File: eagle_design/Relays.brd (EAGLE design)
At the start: 81.3 x 32.7 mm, 13 parts, among them K1 G5LE, K2 G5LE, K3 G5LE

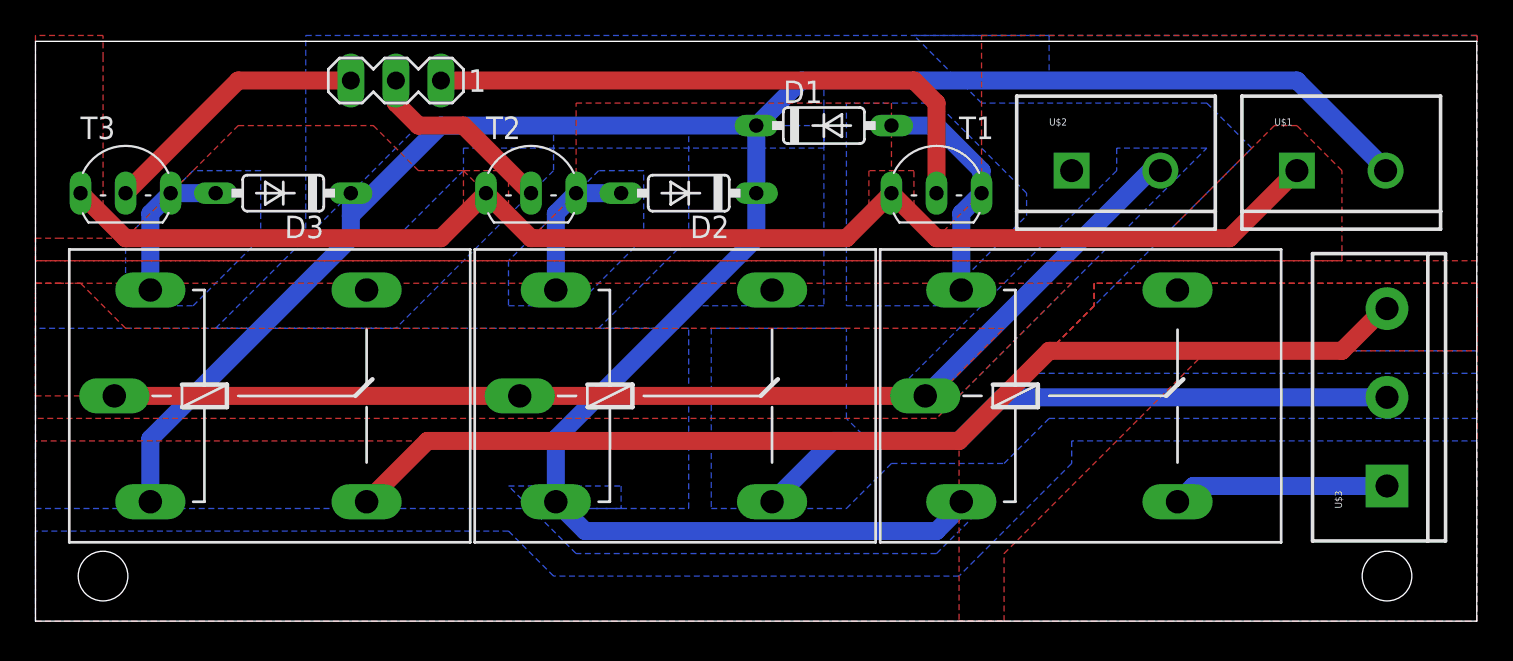
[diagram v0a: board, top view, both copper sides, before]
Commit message: updated schematics
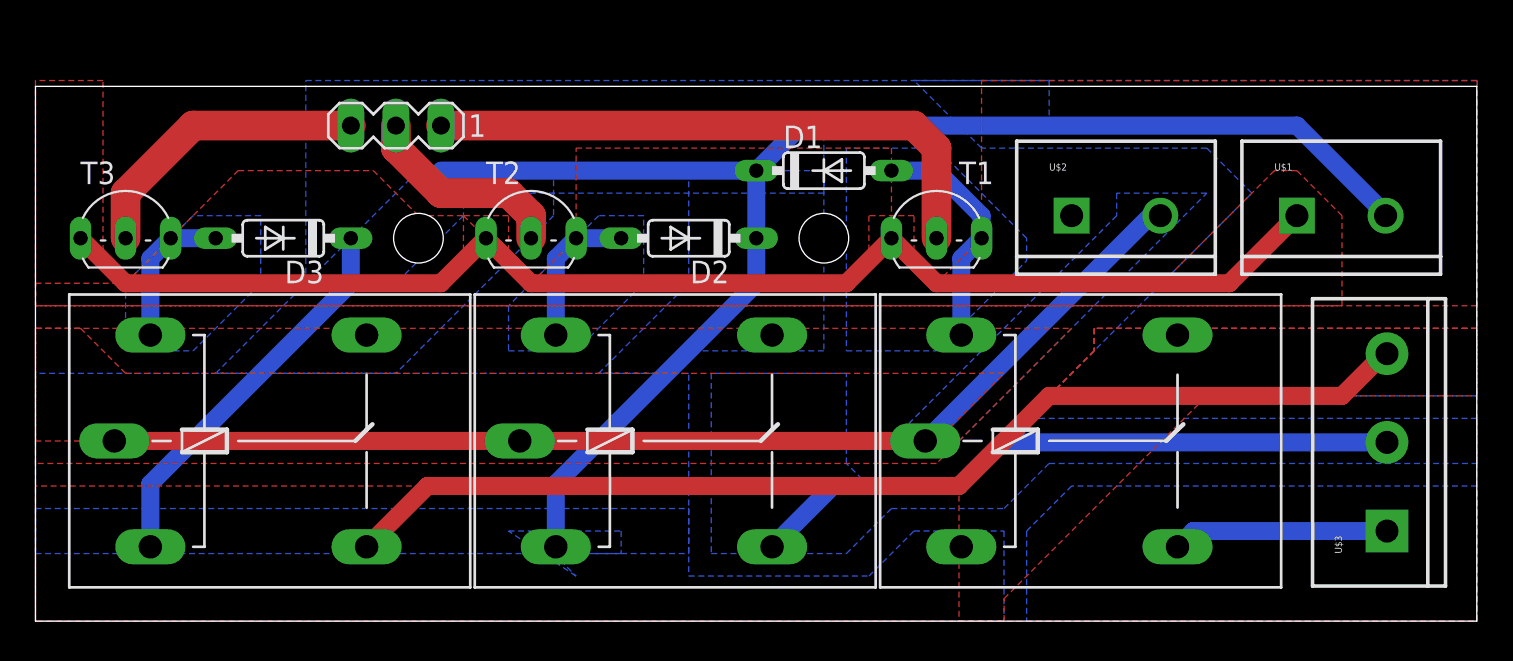
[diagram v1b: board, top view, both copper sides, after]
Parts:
- moved D1 2.54 mm to (44.5, 25.4)
- moved U$3 2.54 mm to (76.2, 5.08)
- moved D2 2.54 mm to (36.8, 21.6)
- moved D3 2.54 mm to (14.0, 21.6)
- moved K1 2.54 mm to (14.0, 10.2)
- moved K2 2.54 mm to (36.8, 10.2)
- moved K3 2.54 mm to (59.7, 10.2)
- moved SV1 2.54 mm to (20.3, 27.9)
- moved T1 2.54 mm to (50.8, 22.9)
- moved T2 2.54 mm to (27.9, 22.9)
- moved T3 2.54 mm to (5.08, 22.9)
- moved U$1 2.54 mm to (71.1, 22.9)
- moved U$2 2.54 mm to (58.4, 22.9)
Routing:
- net FIVE+: track 136.0 -> 104.4 mm
- net HEAT: track 15.3 -> 16.8 mm
- net AC: track 11.0 -> 11.7 mm
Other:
- board size 81.3 x 32.7 mm -> 81.3 x 30.1 mm

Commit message: made boards smaller
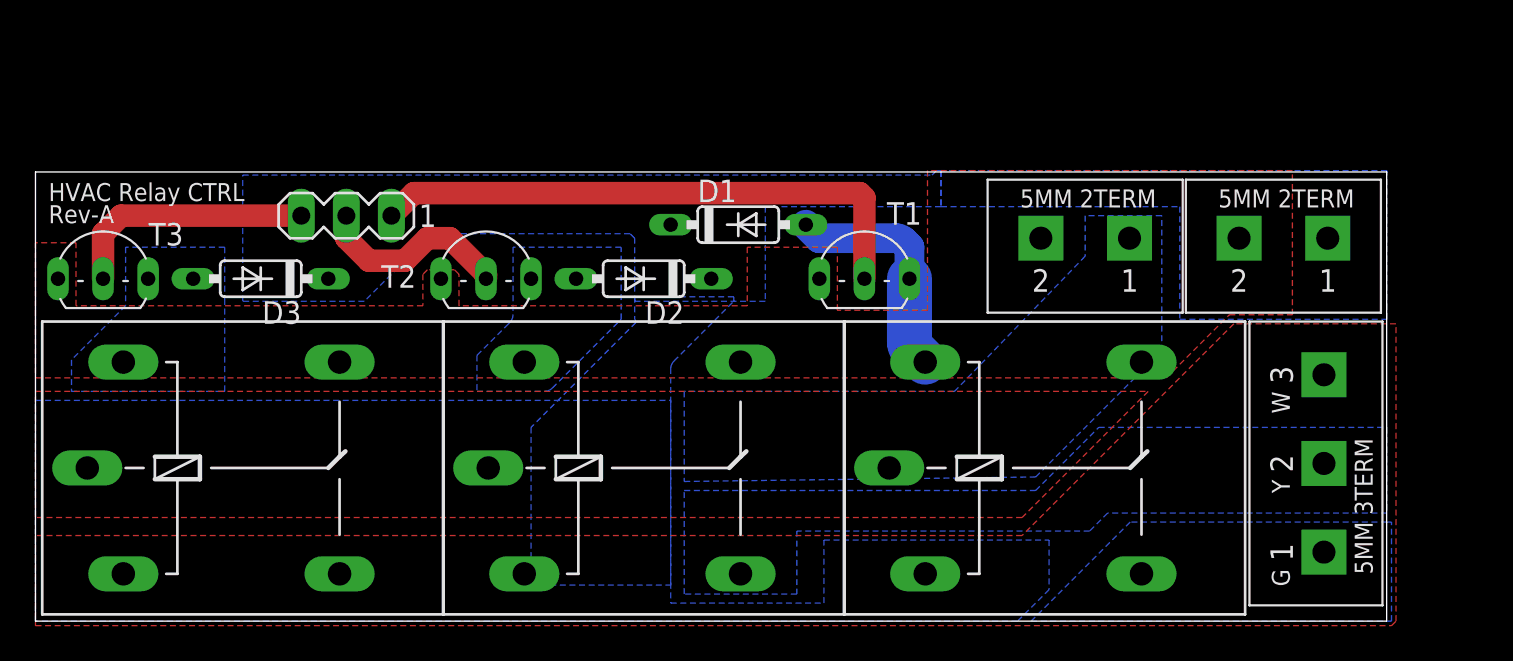
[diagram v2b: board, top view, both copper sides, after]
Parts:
- removed U$1, U$2: SCREWTERMINAL-2, SparkFun-Connectors:SCREWTERMINAL-5MM-2
- removed U$3: SCREWTERMINAL-3, SparkFun-Connectors:SCREWTERMINAL-5MM-3
- added U$4, U$5: OSTTC020162, TylersLib:OSTTC020162
- added U$6: OSTTC030162, TylersLib:OSTTC030162
- moved SV1 5.80 mm to (17.5, 22.9)
- moved D1 5.71 mm to (39.6, 22.4)
- moved T1 4.66 mm to (46.7, 20.6)
- moved D2 3.42 mm to (34.3, 19.3)
- moved T2 3.42 mm to (25.4, 20.6)
- moved D3 2.62 mm to (12.7, 19.3)
- moved T3 2.62 mm to (3.81, 20.6)
- moved K3 2.54 mm to (57.7, 8.64)
- moved K2 2.34 mm to (35.1, 8.64)
- moved K1 2.16 mm to (12.4, 8.64)
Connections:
- net FIVE+: now also U$5.1; no longer U$1.2
- net G: now also U$6.1; no longer U$3.1
- net GND: now also U$5.2; no longer U$1.1
- net VAC+: now also U$4.1; no longer U$2.2
- net VAC-: now also U$4.2; no longer U$2.1
- net W: now also U$6.3; no longer U$3.3
- net Y: now also U$6.2; no longer U$3.2
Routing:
- net FIVE+: track 104.4 -> 0.00 mm
- net GND: track 75.4 -> 0.00 mm
- net VAC+: track 64.2 -> 0.00 mm
- net W: track 62.0 -> 0.00 mm
- net Y: track 37.1 -> 0.00 mm
- net G: track 12.2 -> 0.00 mm
- net N$3: track 8.47 -> 0.00 mm
- net N$5: track 8.47 -> 0.00 mm
- net HEAT: track 16.8 -> 14.1 mm
- net FAN: track 33.5 -> 31.9 mm
- removed copper zone on layer 16, net N$2
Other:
- board size 81.3 x 30.1 mm -> 76.2 x 25.3 mm
- board text added: "G"
- board text added: "HVAC Relay CTRL"
- board text added: "Rev-A"
- board text added: "W"
- board text added: "Y"

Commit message: Cleaned up boards and added script to gen gerbers
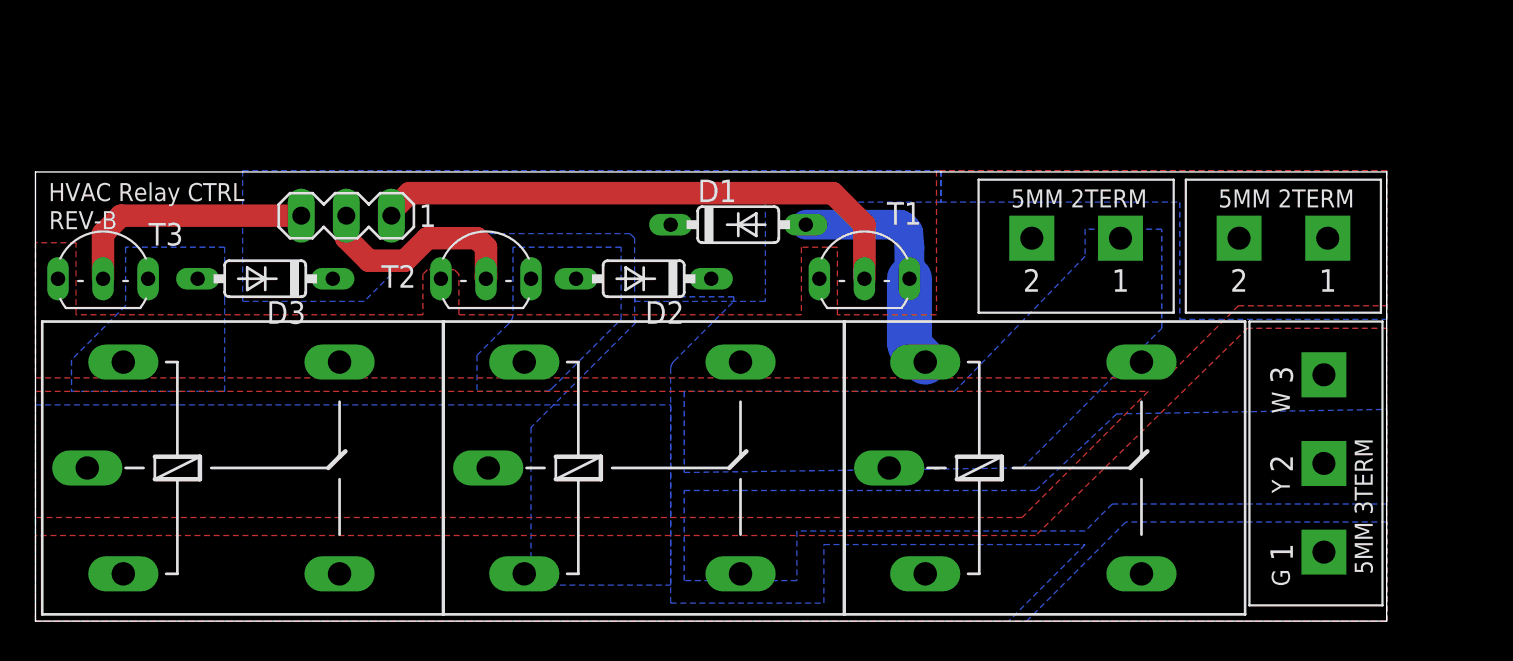
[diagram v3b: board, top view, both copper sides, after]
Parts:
- moved U$4 0.51 mm to (58.7, 21.6)
- moved D3 0.25 mm to (13.0, 19.3)
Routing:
- net AC: track 11.3 -> 12.4 mm
- net FAN: track 31.9 -> 31.1 mm
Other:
- board text added: "5V"
- board text added: "GND"
- board text added: "REV-B"
- board text added: "VAC+"
- board text added: "VAC-"
- board text removed: "Rev-A"
